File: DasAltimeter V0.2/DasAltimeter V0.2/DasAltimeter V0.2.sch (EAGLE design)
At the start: 53 parts, among them IC1 BMI055, U1 ATSAMD21G-A, U2 3.3V/150mA, U3 MS5803-14BA, U4 ADXL193, X1 22-23-2041, X2 22-23-2041

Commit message: playing with mini altimeter idea
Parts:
- removed C9: 0.1uF, SparkFun-Capacitors:0.1UF-0402-16V-10%
- removed H1: STAND-OFFTIGHT, SparkFun-Hardware:STAND-OFFTIGHT
- removed R10, R14: 27k, SparkFun-Resistors:RESISTOR0402
- removed R11, R7: 100, SparkFun-Resistors:RESISTOR0402
- removed R12, R8: 3.3k, SparkFun-Resistors:RESISTOR0402
- removed R13, R9: 100k, SparkFun-Resistors:RESISTOR0402
- removed U$3: SI7232DN, SaL-lib1:SI7232DN
- removed U1: ATSAMD21G-A, SparkFun-IC-Microcontroller:ATSAMD21G-A
- removed U3: MS5803-14BA, SparkFun-Sensors:MS5803-14BA
- removed U4: ADXL193, SparkFun-Sensors:ADXL193
- removed X1: 22-23-2041, con-molex:22-23-2041
- added U$2: ATSAMD10D, SaL-lib1:ATSAMD10D
- added U$5: SIMPLE-MS5607, MS5607:SIMPLE-MS5607
- C3: value 0.1uF -> 100nF
- C5: value 0.1uF -> 4.7uF
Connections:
- removed net FET_C: R9.1, U$3.PIN7, U$3.PIN8, X1-2.S
- removed net FET_D: R13.2, U$3.PIN5, U$3.PIN6, X1-3.S
- removed net FIRE_C: R7.2, R8.1, U1.PA25(SER3:3+)
- removed net FIRE_D: R11.1, R12.2, U1.PA24(SER3:2+)
- removed net N$3: C4.1, U1.VDDCORE
- removed net N$8: R11.2, U$3.PIN4
- removed net SENSE_C: R10.1, R9.2, U1.PA03(AIN1/REFA)
- removed net SENSE_D: R13.1, R14.2, U1.PA02(AIN0/DAC)
- removed net SPI0_MISO: IC1.SDO1, IC1.SDO2, U1.PA11(AIN19/SER0:3+)
- removed net SPI0_MOSI: IC1.SDX, U1.PA08(I2C/AIN16/SER0:0+)
- removed net SPI0_SCK: IC1.SCX, U1.PA09(I2C/AIN17/SER0:1+)
- removed net SPI2_MISO: U1.PA13(I2C/SER2:1+), U3.SDO
- removed net SPI2_MOSI: U1.PA12(I2C/SER2:0+), U3.SDA/SDI
- removed net SPI2_SCK: U1.PA15(XOUT/SER2:3+), U3.SCL/SCLK
- net !RESET: now also U$2.PA28(!RESET!); no longer U1.!RESET!
- net 3.3V: now also C4.1; no longer C3.1, C9.1, U1.VDDIN, U1.VDDIO@17, U1.VDDIO@36, U3.VDD, U4.VDD, U4.VDD2
- net ACCELX: now also U$2.PA07(AIN[5]/SER0:1); no longer U1.PA07(AIN7/SER0:3/TC1:1), U4.OUT
- net BUZZER: now also U$2.PA11(AIN[9]/SER0:3); no longer U1.PA21(SER5:3+)
- net CS_ACCEL: now also U$2.PA14(AIN[6]/SER0:0); no longer U1.PB10(SER4:2+)
- net CS_BARO: now also U$2.PA27, U$5.CSB2; no longer U1.PA14(XIN/SER2:2+), U3.AD/CS
- net CS_GYRO: now also U$2.PA15(AIN[7]/SER0:1); no longer U1.PA10(AIN18/SER0:2+)
- net CS_MEM: now also U$2.PA16(SER1:2); no longer U1.PA18(SER1:2+)
- net FIRE_A: now also U$2.PA09(SER1:3); no longer U1.PB23(SER5:3+)
- net FIRE_B: now also U$2.PA08(SER1:2); no longer U1.PB22(SER5:2+)
- net GND: now also U$2.GND@23, U$5.GND; no longer C4.2, C9.2, R10.2, R12.1, R14.1, R8.2, U$3.PIN1, U$3.PIN3, U1.GND@18, U1.GND@35, U1.GND@42, U1.GNDANA, U3.GND, U3.PS, U4.GND
- net LED: now also U$2.PA10(AIN[8]/SER0:2); no longer U1.PA20(SER5:2+)
- net N$1: now also C4.2, U$5.VDD; no longer R7.1, U$3.PIN2
- net N$4: now also C3.1, U$2.VDDIN; no longer U1.VDDANA
- net RX: now also U$2.PA25(SER1:3); no longer U1.PA23(I2C/SER3:0+)
- net SENSE_A: now also U$2.PA02(ANI[0]/DAC); no longer U1.PB03(AIN11/SER5:1)
- net SENSE_B: now also U$2.PA03(AIN[1]/REFA); no longer U1.PB02(AIN10/SER5:0)
- net SENSE_BAT: now also U$2.PA06(AIN[4]/SER0:0); no longer U1.PA06(AIN6/SER0:2/TC1:0)
- net SPI1_MISO: now also IC1.SDO1, IC1.SDO2, U$2.PA17(SER1:3); no longer U1.PA19(SER1:3+)
- net SPI1_MOSI: now also IC1.SDX, U$2.PA22(SER1:0); no longer U1.PA16(I2C/SER1:0+)
- net SPI1_SCK: now also IC1.SCX, U$2.PA23(SER1:1); no longer U1.PA17(I2C/SER1:1+)
- net SWCLK: now also U$2.PA30(SWCLK/SER1:0); no longer U1.PA30(SWCLK/SER1:2+)
- net SWDIO: now also U$2.PA31(SWDOI/SER1:1); no longer U1.PA31(SWDIO/SER1:3+)
- net TX: now also U$2.PA24(SER1:2); no longer U1.PA22(I2C/SER3:0+)
- net VCC: no longer X1-1.S, X1-4.S
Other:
- moved on the sheet: C10, C11, C3, C4, C5, IC1, L1, R1, R23, R24, R4, X2-1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

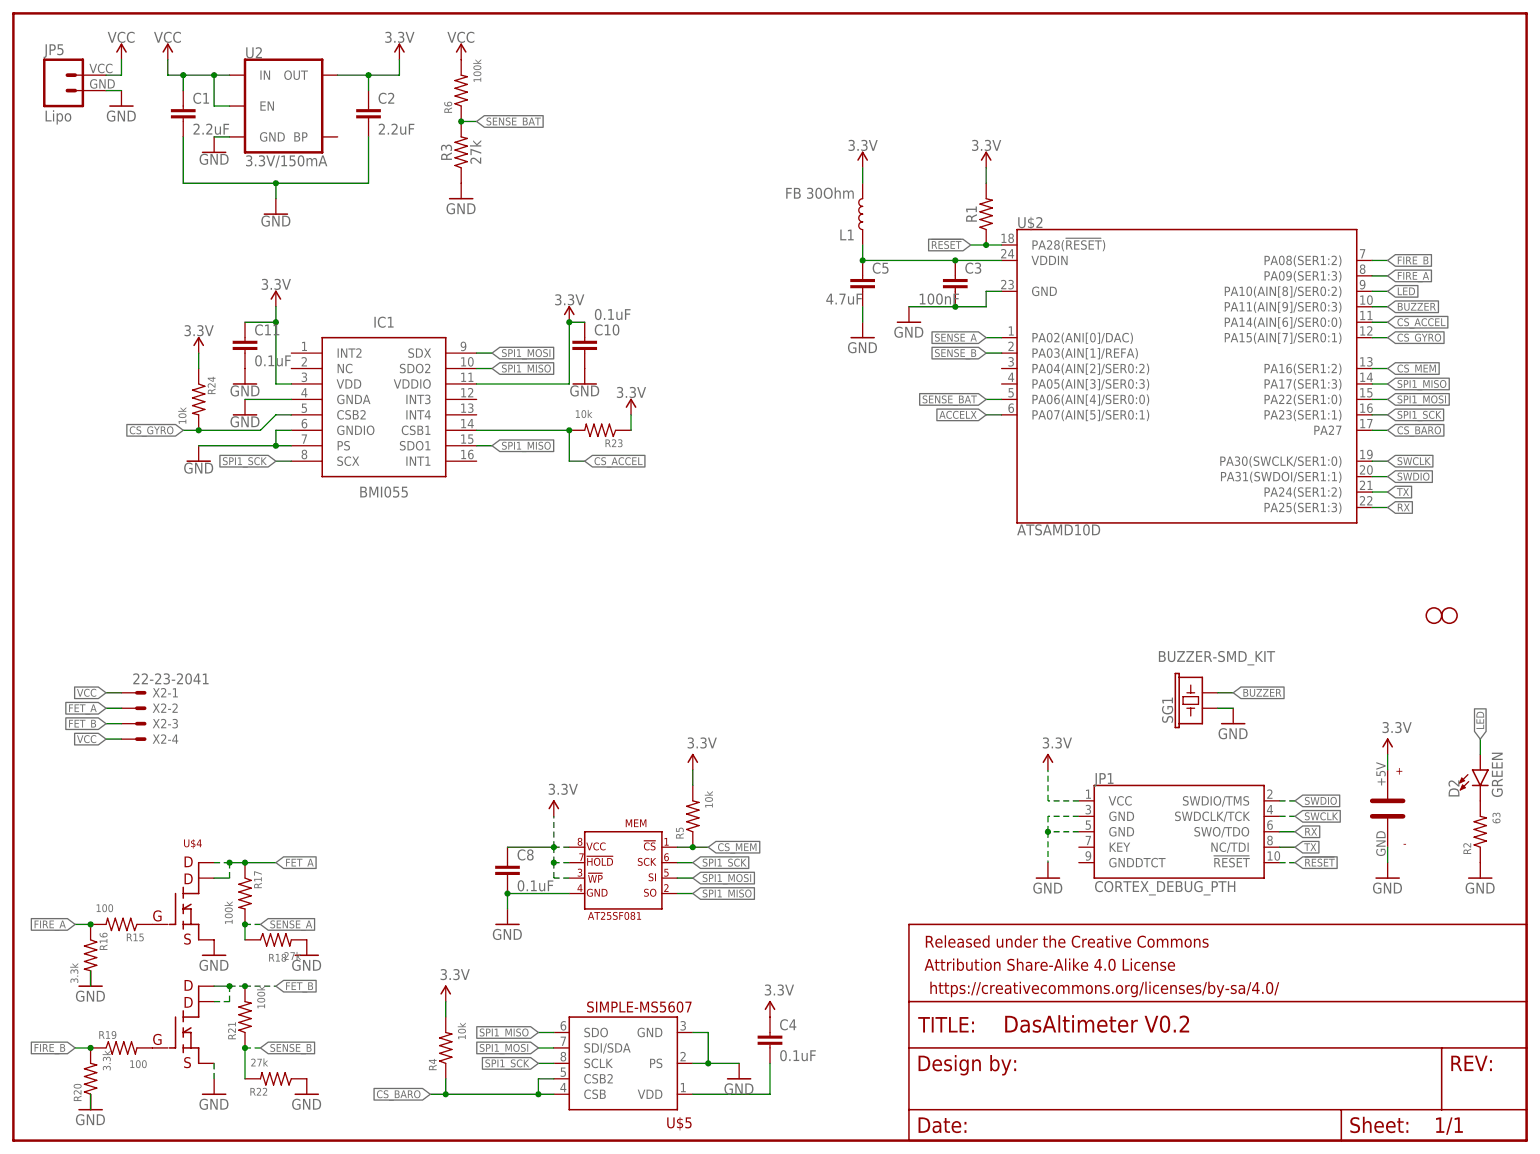
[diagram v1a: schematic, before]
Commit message: Revert "playing with mini altimeter idea"
This reverts commit 0304c3ccd9bbc4967d121740b09f5fd7c2a4b911.
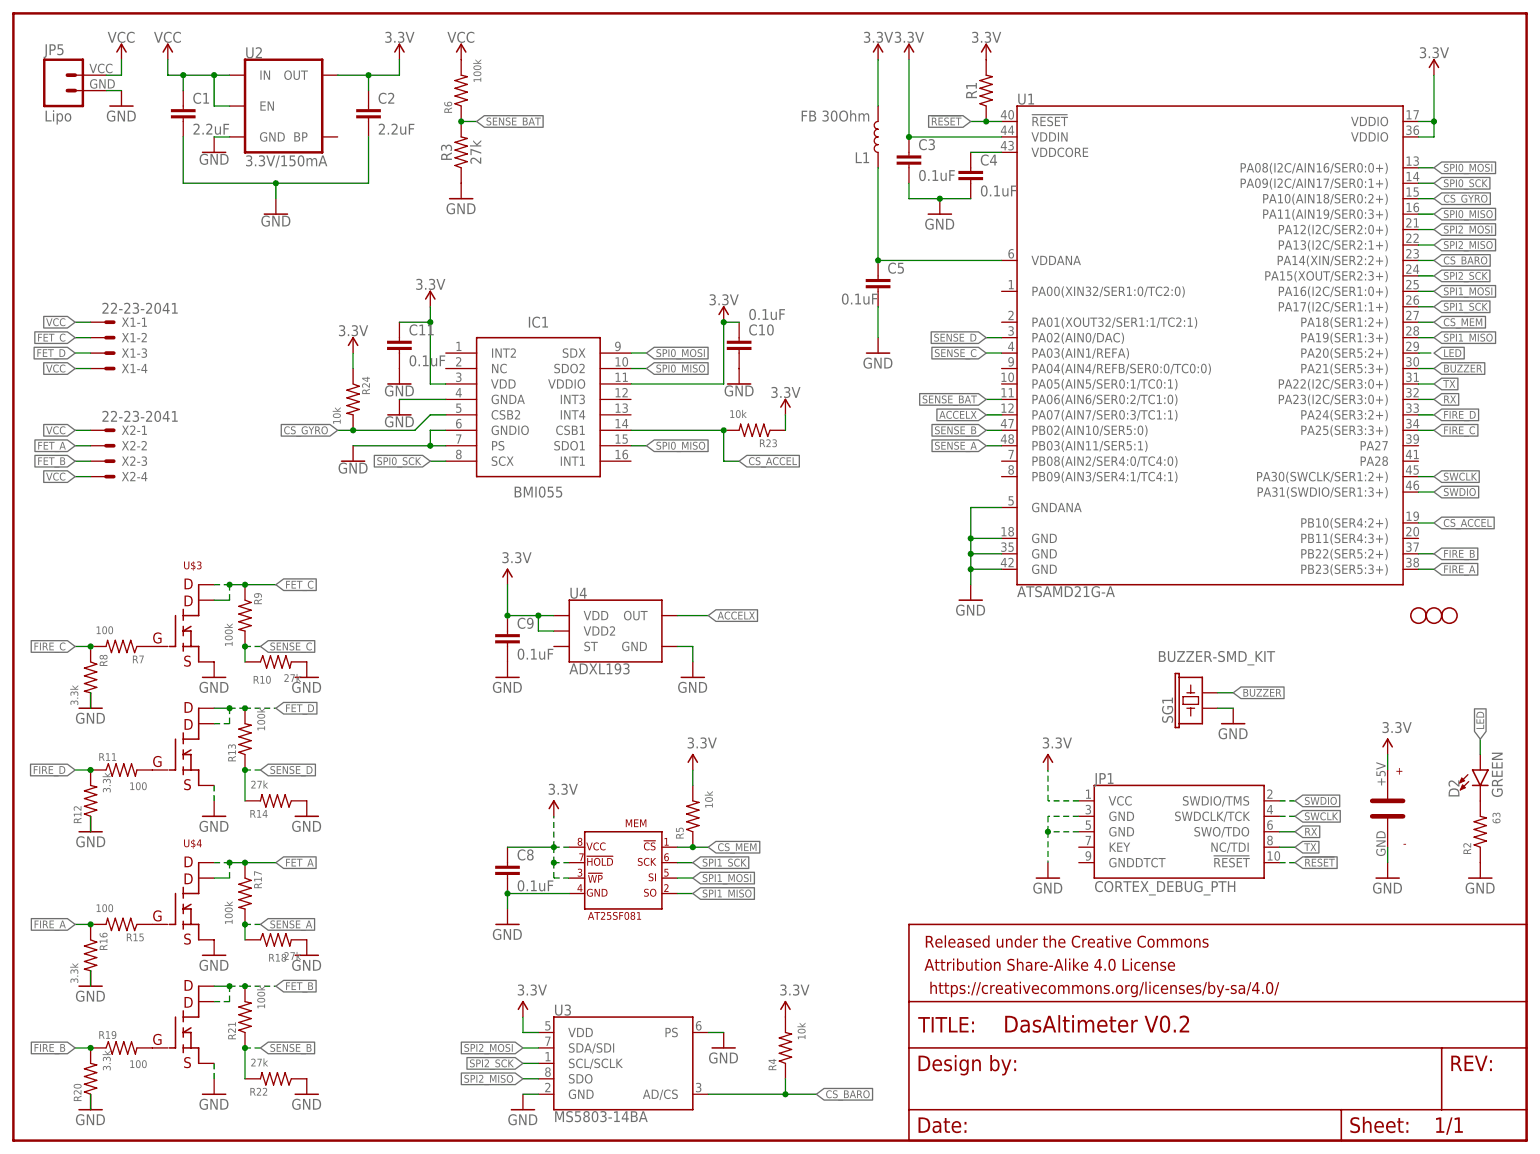
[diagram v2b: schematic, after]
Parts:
- removed U$2: ATSAMD10D, SaL-lib1:ATSAMD10D
- removed U$5: SIMPLE-MS5607, MS5607:SIMPLE-MS5607
- added C9: 0.1uF, SparkFun-Capacitors:0.1UF-0402-16V-10%
- added H1: STAND-OFFTIGHT, SparkFun-Hardware:STAND-OFFTIGHT
- added R10, R14: 27k, SparkFun-Resistors:RESISTOR0402
- added R11, R7: 100, SparkFun-Resistors:RESISTOR0402
- added R12, R8: 3.3k, SparkFun-Resistors:RESISTOR0402
- added R13, R9: 100k, SparkFun-Resistors:RESISTOR0402
- added U$3: SI7232DN, SaL-lib1:SI7232DN
- added U1: ATSAMD21G-A, SparkFun-IC-Microcontroller:ATSAMD21G-A
- added U3: MS5803-14BA, SparkFun-Sensors:MS5803-14BA
- added U4: ADXL193, SparkFun-Sensors:ADXL193
- added X1: 22-23-2041, con-molex:22-23-2041
- C3: value 100nF -> 0.1uF
- C5: value 4.7uF -> 0.1uF
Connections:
- new net FET_C: R9.1, U$3.PIN7, U$3.PIN8, X1-2.S
- new net FET_D: R13.2, U$3.PIN5, U$3.PIN6, X1-3.S
- new net FIRE_C: R7.2, R8.1, U1.PA25(SER3:3+)
- new net FIRE_D: R11.1, R12.2, U1.PA24(SER3:2+)
- new net N$3: C4.1, U1.VDDCORE
- new net N$8: R11.2, U$3.PIN4
- new net SENSE_C: R10.1, R9.2, U1.PA03(AIN1/REFA)
- new net SENSE_D: R13.1, R14.2, U1.PA02(AIN0/DAC)
- new net SPI0_MISO: IC1.SDO1, IC1.SDO2, U1.PA11(AIN19/SER0:3+)
- new net SPI0_MOSI: IC1.SDX, U1.PA08(I2C/AIN16/SER0:0+)
- new net SPI0_SCK: IC1.SCX, U1.PA09(I2C/AIN17/SER0:1+)
- new net SPI2_MISO: U1.PA13(I2C/SER2:1+), U3.SDO
- new net SPI2_MOSI: U1.PA12(I2C/SER2:0+), U3.SDA/SDI
- new net SPI2_SCK: U1.PA15(XOUT/SER2:3+), U3.SCL/SCLK
- net !RESET: now also U1.!RESET!; no longer U$2.PA28(!RESET!)
- net 3.3V: now also C3.1, C9.1, U1.VDDIN, U1.VDDIO@17, U1.VDDIO@36, U3.VDD, U4.VDD, U4.VDD2; no longer C4.1
- net ACCELX: now also U1.PA07(AIN7/SER0:3/TC1:1), U4.OUT; no longer U$2.PA07(AIN[5]/SER0:1)
- net BUZZER: now also U1.PA21(SER5:3+); no longer U$2.PA11(AIN[9]/SER0:3)
- net CS_ACCEL: now also U1.PB10(SER4:2+); no longer U$2.PA14(AIN[6]/SER0:0)
- net CS_BARO: now also U1.PA14(XIN/SER2:2+), U3.AD/CS; no longer U$2.PA27, U$5.CSB2
- net CS_GYRO: now also U1.PA10(AIN18/SER0:2+); no longer U$2.PA15(AIN[7]/SER0:1)
- net CS_MEM: now also U1.PA18(SER1:2+); no longer U$2.PA16(SER1:2)
- net FIRE_A: now also U1.PB23(SER5:3+); no longer U$2.PA09(SER1:3)
- net FIRE_B: now also U1.PB22(SER5:2+); no longer U$2.PA08(SER1:2)
- net GND: now also C4.2, C9.2, R10.2, R12.1, R14.1, R8.2, U$3.PIN1, U$3.PIN3, U1.GND@18, U1.GND@35, U1.GND@42, U1.GNDANA, U3.GND, U3.PS, U4.GND; no longer U$2.GND@23, U$5.GND
- net LED: now also U1.PA20(SER5:2+); no longer U$2.PA10(AIN[8]/SER0:2)
- net N$1: now also R7.1, U$3.PIN2; no longer C4.2, U$5.VDD
- net N$4: now also U1.VDDANA; no longer C3.1, U$2.VDDIN
- net RX: now also U1.PA23(I2C/SER3:0+); no longer U$2.PA25(SER1:3)
- net SENSE_A: now also U1.PB03(AIN11/SER5:1); no longer U$2.PA02(ANI[0]/DAC)
- net SENSE_B: now also U1.PB02(AIN10/SER5:0); no longer U$2.PA03(AIN[1]/REFA)
- net SENSE_BAT: now also U1.PA06(AIN6/SER0:2/TC1:0); no longer U$2.PA06(AIN[4]/SER0:0)
- net SPI1_MISO: now also U1.PA19(SER1:3+); no longer IC1.SDO1, IC1.SDO2, U$2.PA17(SER1:3)
- net SPI1_MOSI: now also U1.PA16(I2C/SER1:0+); no longer IC1.SDX, U$2.PA22(SER1:0)
- net SPI1_SCK: now also U1.PA17(I2C/SER1:1+); no longer IC1.SCX, U$2.PA23(SER1:1)
- net SWCLK: now also U1.PA30(SWCLK/SER1:2+); no longer U$2.PA30(SWCLK/SER1:0)
- net SWDIO: now also U1.PA31(SWDIO/SER1:3+); no longer U$2.PA31(SWDOI/SER1:1)
- net TX: now also U1.PA22(I2C/SER3:0+); no longer U$2.PA24(SER1:2)
- net VCC: now also X1-1.S, X1-4.S
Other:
- moved on the sheet: C10, C11, C3, C4, C5, IC1, L1, R1, R23, R24, R4, X2-1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
